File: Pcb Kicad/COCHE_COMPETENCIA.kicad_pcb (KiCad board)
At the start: 2 copper layers, 95 x 62 mm, 39 parts, among them J1 BAT, J2 SWITCH, J4 M1, J5 M2, J6 SENSORES, Q1 2N3904, SW1 SW_Push, SW2 SW_Push, U2 ESP32-DEVKIT-V1, U3 DRV8833, U4 DRV8833, U5 AMS1117

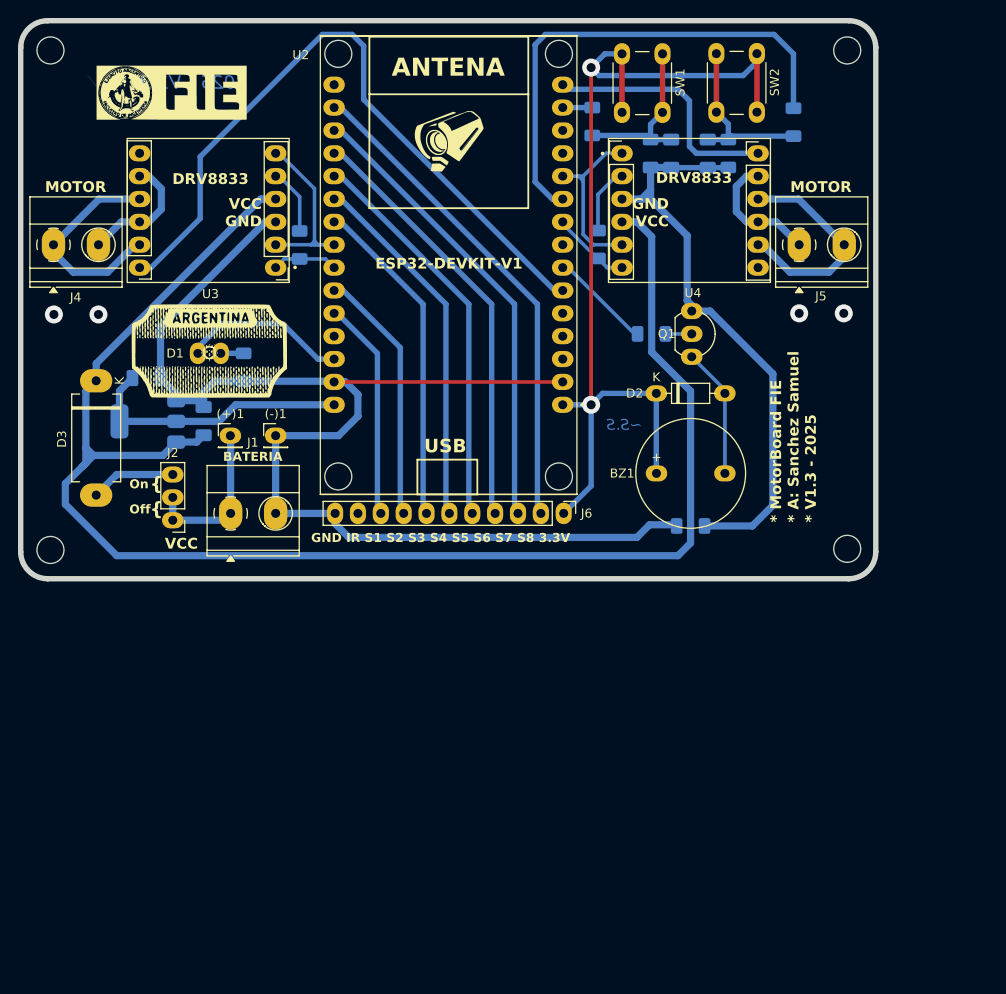
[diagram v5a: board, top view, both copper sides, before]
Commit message: V1.4 - Mejores pistas & Modulo de Interrupciones
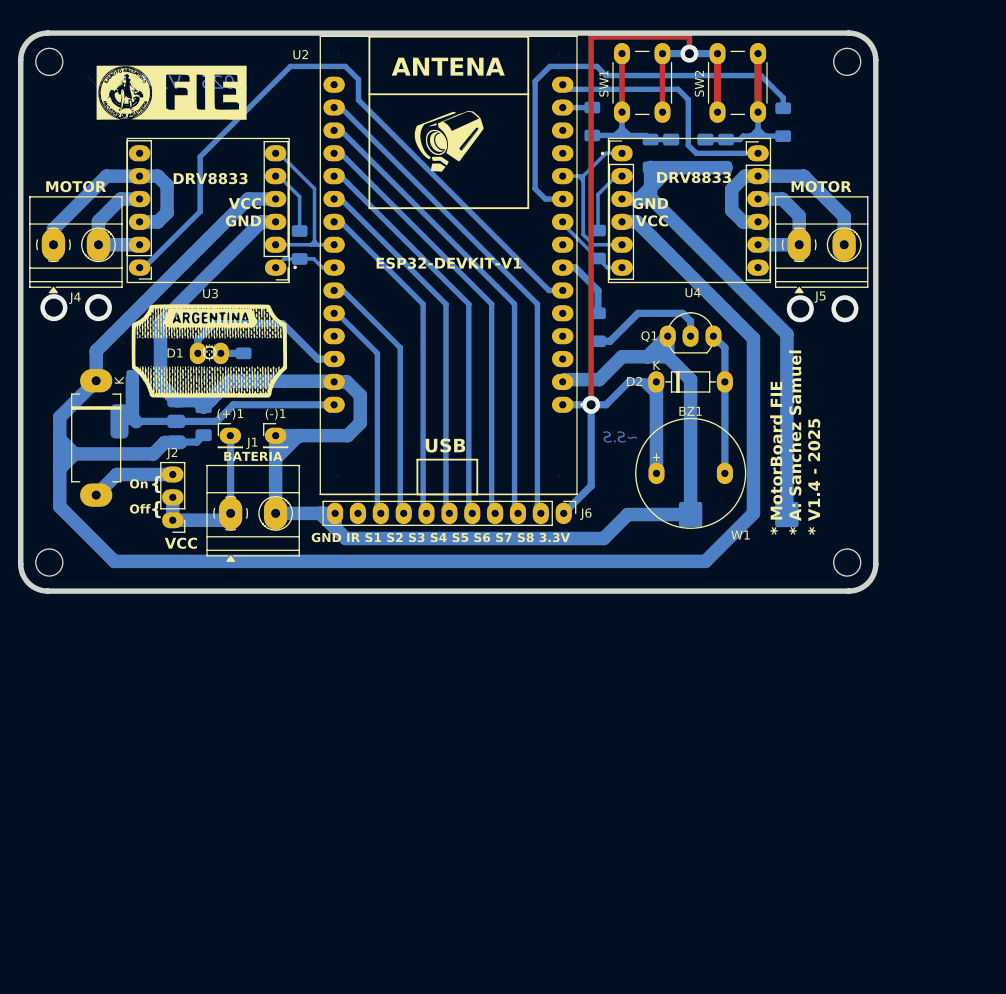
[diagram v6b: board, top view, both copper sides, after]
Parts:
- removed R1: 0, Resistor_SMD:R_1206_3216Metric_Pad1.30x1.75mm_HandSolder
- added W1: 5104, JUMPLER 5104:KEYSTONE_5104, B.Cu at (177.4, 79.1)
- moved SW1 7.92 mm to (169.0, 27.9), turned to -90 degrees
- moved SW2 7.83 mm to (175.1, 34.4), turned to 90 degrees
- moved R7 5.99 mm to (161.8, 58.3), turned to -90 degrees
- moved Q1 3.86 mm to (169.5, 59.3), turned to 0 degrees
- moved H4 1.52 mm to (189.5, 84.5)
- moved H3 1.40 mm to (100.8, 84.5)
- moved H1 1.28 mm to (100.8, 28.8)
- moved D2 1.27 mm to (168.3, 64.4)
- moved H2 1.27 mm to (189.5, 28.8)
- moved R8 1.14 mm to (182.4, 35.5)
- moved C4 0.25 mm to (173.7, 39.0)
- moved R3 0.25 mm to (176.0, 39.0)
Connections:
- U3 pad 10: Net-(J4-Pin_2) -> Net-(J4-Pin_1)
- U3 pad 11: Net-(J4-Pin_1) -> Net-(J4-Pin_2)
- U3 pad 8: Net-(J4-Pin_2) -> Net-(J4-Pin_1)
- U3 pad 9: Net-(J4-Pin_1) -> Net-(J4-Pin_2)
- U4 pad 10: Net-(J5-Pin_2) -> Net-(J5-Pin_1)
- U4 pad 11: Net-(J5-Pin_1) -> Net-(J5-Pin_2)
- U4 pad 8: Net-(J5-Pin_2) -> Net-(J5-Pin_1)
- U4 pad 9: Net-(J5-Pin_1) -> Net-(J5-Pin_2)
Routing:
- net GND: track 208.9 -> 226.8 mm
- net VCC: track 172.8 -> 189.0 mm
- net Net-(Q1-B): track 2.92 -> 13.6 mm
- net /SW2: track 55.2 -> 46.3 mm
- net /SLEEP_M1: track 77.0 -> 71.5 mm
- net /BUZZER: track 12.6 -> 9.37 mm
- net +3.3V: track 108.0 -> 110.3 mm
- net Net-(BZ1--): track 14.5 -> 15.8 mm
- net Net-(J4-Pin_2): track 13.9 -> 12.8 mm
- net Net-(J5-Pin_1): track 14.2 -> 13.1 mm
- net Net-(C3-Pad1): track 19.6 -> 20.3 mm
- net Net-(J5-Pin_2): track 24.6 -> 23.9 mm
- net Net-(C4-Pad1): track 19.8 -> 20.4 mm
- net /LED_LARGADA: track 18.5 -> 19.0 mm
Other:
- board text added: "* MotorBoard FIE * A: Sanchez Samuel * V1.4 - 2025"
- board text added: "2025 - V1.4"
- board text removed: "* MotorBoard FIE * A: Sanchez Samuel * V1.3 - 2025"
- board text removed: "2025 - V1.3"

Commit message: V1.4 - Programa seguidor Modular
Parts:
- moved R7 2.12 mm to (163.3, 56.8), turned to 0 degrees
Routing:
- net GND: track 226.8 -> 210.8 mm
- net Net-(Q1-B): track 13.6 -> 9.27 mm
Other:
- board text added: "* MotorBoard FIE * A: Sanchez Samuel * V1.5 - 2025"
- board text removed: "* MotorBoard FIE * A: Sanchez Samuel * V1.4 - 2025"
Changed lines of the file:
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@@
 	(footprint "Resistor_SMD:R_1206_3216Metric_Pad1.30x1.75mm_HandSolder"
 		(layer "B.Cu")
-		(at 161.798 58.319 -90)
+		(at 163.2972 56.8198)
 		(descr "Resistor SMD 1206 (3216 Metric), square (rectangular) end terminal, IPC_7351 nominal with elongated pad for handsoldering. (Body size source: IPC-SM-782 page 72, https://www.pcb-3d.com/wordpress/wp-content/uploads/ipc-sm-782a_amendment_1_and_2.pdf), generated with kicad-footprint-generator")
 		(tags "resistor handsolder")
 		(property "Reference" "R7"
-			(at 3.2252 0 180)
+			(at 3.2252 0 90)
 			(layer "B.SilkS")
 			(effects
@@
 		)
 		(property "Value" "1k"
-			(at 3.1236 0 180)
+			(at 3.1236 0 90)
 			(layer "B.Fab")
 			(effects
@@
 		)
 		(property "Datasheet" ""
-			(at 0 0 90)
+			(at 0 0 180)
 			(unlocked yes)
 			(layer "B.Fab")
@@
 		)
 		(property "Description" "Resistor"
-			(at 0 0 90)
+			(at 0 0 180)
 			(unlocked yes)
 			(layer "B.Fab")
@@
 		(attr smd)
 		(fp_line
-			(start -0.727064 0.91)
-			(end 0.727064 0.91)
+			(start -0.727064 -0.91)
+			(end 0.727064 -0.91)
 			(stroke
 				(width 0.12)
@@
 		)
 		(fp_line
-			(start -0.727064 -0.91)
-			(end 0.727064 -0.91)
+			(start -0.727064 0.91)
+			(end 0.727064 0.91)
 			(stroke
 				(width 0.12)
@@
 		)
 		(fp_line
-			(start -2.45 1.12)
-			(end 2.45 1.12)
+			(start -2.45 -1.12)
+			(end -2.45 1.12)
 			(stroke
 				(width 0.05)
@@
 		)
 		(fp_line
-			(start 2.45 1.12)
-			(end 2.45 -1.12)
+			(start -2.45 1.12)
+			(end 2.45 1.12)
 			(stroke
 				(width 0.05)
@@
 		)
 		(fp_line
-			(start -2.45 -1.12)
-			(end -2.45 1.12)
+			(start 2.45 -1.12)
+			(end -2.45 -1.12)
 			(stroke
 				(width 0.05)
@@
 		)
 		(fp_line
-			(start 2.45 -1.12)
-			(end -2.45 -1.12)
+			(start 2.45 1.12)
+			(end 2.45 -1.12)
 			(stroke
 				(width 0.05)
@@
 		)
 		(fp_line
-			(start -1.6 0.8)
-			(end 1.6 0.8)
+			(start -1.6 -0.8)
+			(end -1.6 0.8)
 			(stroke
 				(width 0.1)
@@
 		)
 		(fp_line
-			(start 1.6 0.8)
-			(end 1.6 -0.8)
+			(start -1.6 0.8)
+			(end 1.6 0.8)
 			(stroke
 				(width 0.1)
@@
 		)
 		(fp_line
-			(start -1.6 -0.8)
-			(end -1.6 0.8)
+			(start 1.6 -0.8)
+			(end -1.6 -0.8)
 			(stroke
 				(width 0.1)
@@
 		)
 		(fp_line
-			(start 1.6 -0.8)
-			(end -1.6 -0.8)
+			(start 1.6 0.8)
+			(end 1.6 -0.8)
 			(stroke
 				(width 0.1)
@@
 		)
 		(fp_text user "${REFERENCE}"
-			(at 0 0 90)
+			(at 0 0 0)
 			(layer "B.Fab")
 			(effects
@@
 		)
 		(pad "1" smd roundrect
-			(at -1.55 0 270)
+			(at -1.55 0)
 			(size 1.3 1.75)
 			(layers "B.Cu" "B.Mask" "B.Paste")
@@
 		)
 		(pad "2" smd roundrect
-			(at 1.55 0 270)
+			(at 1.55 0)
 			(size 1.3 1.75)
 			(layers "B.Cu" "B.Mask" "B.Paste")
@@
 		)
 	)
-	(gr_text "* MotorBoard FIE\n* A: Sanchez Samuel\n* V1.4 - 2025"
+	(gr_text "* MotorBoard FIE\n* A: Sanchez Samuel\n* V1.5 - 2025"
 		(at 183.769 81.407 90)
 		(layer "F.SilkS")
@@
 	)
 	(segment
-		(start 169.545 59.309)
-		(end 167.259 61.595)
-		(width 1.5)
-		(layer "B.Cu")
-		(net 7)
-	)
-	(segment
 		(start 133.788 81.788)
 		(end 132.588 80.588)
@@
 	)
 	(segment
-		(start 167.259 61.595)
-		(end 169.545 61.595)
-		(width 1.5)
-		(layer "B.Cu")
-		(net 7)
-	)
-	(segment
-		(start 157.877 64.389)
-		(end 158.131 64.135)
-		(width 1.5)
-		(layer "B.Cu")
-		(net 7)
-	)
-	(segment
 		(start 118.696 66.47)
 		(end 118.872 66.294)
@@
 	)
 	(segment
-		(start 164.465 61.595)
-		(end 167.259 61.595)
-		(width 1.5)
-		(layer "B.Cu")
-		(net 7)
-	)
-	(segment
 		(start 132.531 80.588)
 		(end 130.937 78.994)
@@
 	)
 	(segment
-		(start 158.131 64.135)
-		(end 161.925 64.135)
-		(width 1.5)
-		(layer "B.Cu")
-		(net 7)
-	)
-	(segment
-		(start 161.925 64.135)
-		(end 164.465 61.595)
-		(width 1.5)
-		(layer "B.Cu")
-		(net 7)
-	)
-	(segment
 		(start 120.852 64.314)
 		(end 122.428 64.314)
@@
 		(start 171.958 26.035)
 		(end 161.036 26.035)
-		(width 0.6)
+		(width 0.8)
 		(layer "F.Cu")
 		(net 17)
@@
 		(start 171.958 27.917)
 		(end 171.958 26.035)
-		(width 0.6)
+		(width 0.8)
 		(layer "F.Cu")
 		(net 17)
@@
 		(start 161.036 26.035)
 		(end 161.036 66.929)
-		(width 0.6)
+		(width 0.8)
 		(layer "F.Cu")
 		(net 17)
@@
 		(start 168.295 66.04)
 		(end 168.295 64.409)
-		(width 1.5)
+		(width 0.8)
 		(layer "B.Cu")
 		(net 17)
@@
 		(start 168.295 74.549)
 		(end 168.295 66.04)
-		(width 1.5)
+		(width 0.8)
 		(layer "B.Cu")
 		(net 17)
@@
 		(start 168.295 64.409)
 		(end 168.275 64.389)
-		(width 1.5)
+		(width 0.8)
 		(layer "B.Cu")
 		(net 17)
@@
 	)
 	(segment
+		(start 161.7472 54.1782)
+		(end 161.7472 56.8198)
+		(width 0.8)
+		(layer "B.Cu")
+		(net 28)
+	)
+	(segment
 		(start 157.877 51.689)
 		(end 158.242 51.689)
@@
 	)
 	(segment
-		(start 161.798 56.769)
-		(end 161.798 54.229)
+		(start 161.1376 53.5686)
+		(end 159.258 51.689)
 		(width 0.8)
 		(layer "B.Cu")
@@
 	(segment
 		(start 161.798 54.229)
-		(end 159.258 51.689)
+		(end 161.1376 53.5686)
 		(width 0.8)
 		(layer "B.Cu")
@@
 	)
 	(segment
-		(start 171.196 56.769)
-		(end 172.085 57.658)
+		(start 164.8472 56.8198)
+		(end 171.2468 56.8198)
 		(width 0.8)
 		(layer "B.Cu")
@@
 	(segment
 		(start 172.085 57.658)
-		(end 172.085 59.309)
-		(width 0.8)
-		(layer "B.Cu")
-		(net 42)
-	)
-	(segment
-		(start 163.143 59.869)
-		(end 166.243 56.769)
+		(end 171.2214 56.7944)
 		(width 0.8)
 		(layer "B.Cu")
@@
 	)
 	(segment
-		(start 166.243 56.769)
-		(end 171.196 56.769)
-		(width 0.8)
-		(layer "B.Cu")
-		(net 42)
-	)
-	(segment
-		(start 161.798 59.869)
-		(end 163.143 59.869)
+		(start 172.085 59.309)
+		(end 172.085 57.658)
 		(width 0.8)
 		(layer "B.Cu")

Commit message: V2.0 - Nueva version Seguidor De Linea
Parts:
- removed (+)1, (-)1: TestPoint, Connector_PinHeader_2.54mm:PinHeader_1x01_P2.54mm_Vertical
- removed BZ1: Buzzer, Buzzer_Beeper:MagneticBuzzer_ProSignal_ABI-009-RC
- removed C4: 100n, Capacitor_SMD:C_1206_3216Metric_Pad1.33x1.80mm_HandSolder
- removed D2: 1N4148, Diode_THT:D_DO-35_SOD27_P7.62mm_Horizontal
- removed D3: 1N5822, Diode_THT:D_DO-201AD_P12.70mm_Horizontal
- removed H1, H2, H3, H4: MountingHole, MountingHole:MountingHole_3mm
- removed J2: SWITCH, Connector_PinHeader_2.54mm:PinHeader_1x03_P2.54mm_Vertical
- removed J4: M1, TerminalBlock_Phoenix:TerminalBlock_Phoenix_MKDS-1,5-2_1x02_P5.00mm_Horizontal
- removed Q1: 2N3904, Package_TO_SOT_THT:TO-92_Inline_Wide
- removed R2, R3: 10k, Resistor_SMD:R_1206_3216Metric_Pad1.30x1.75mm_HandSolder
- removed R4: 220, Resistor_SMD:R_1206_3216Metric_Pad1.30x1.75mm_HandSolder
- removed R5, R6: 0, Resistor_SMD:R_1206_3216Metric_Pad1.30x1.75mm_HandSolder
- removed R7: 1k, Resistor_SMD:R_1206_3216Metric_Pad1.30x1.75mm_HandSolder
- removed R8, R9: 100, Resistor_SMD:R_1206_3216Metric_Pad1.30x1.75mm_HandSolder
- removed U3, U4: DRV8833, DRV8833:DRV8833
- removed U5: AMS1117, Package_TO_SOT_SMD:SOT-223-3_TabPin2
- removed W1: 5104, JUMPLER 5104:KEYSTONE_5104
- added BT1: 2S 70C 250mAH, Bateria_9S:Bateria_Lado, F.Cu at (167.4, 102.7)
- added J3: SENSORES, Connector_PinHeader_2.54mm:PinHeader_1x11_P2.54mm_Vertical, F.Cu at (180.1, 68.4)
- added M1: Pololu DC, PololuLibrary:pololu, F.Cu at (154.1, 117.4)
- added M2: Pololu DC, PololuLibrary:pololu, F.Cu at (180.8, 117.4)
- added U1: DRV8833, DRV8833:DRV8833, F.Cu at (135.3, 84.3)
- C2: value 1u -> 100n
- D1: value LED_RED -> D_Schottky; footprint LED_THT:LED_D5.0mm -> Diode_THT:D_DO-35_SOD27_P7.62mm_Horizontal
- J1: footprint TerminalBlock_Phoenix:TerminalBlock_Phoenix_MKDS-1,5-2_1x02_P5.00mm_Horizontal -> Connector_AMASS:AMASS_XT30UPB-M_1x02_P5.0mm_Vertical
- J5: value M2 -> M1; footprint TerminalBlock_Phoenix:TerminalBlock_Phoenix_MKDS-1,5-2_1x02_P5.00mm_Horizontal -> Connector_PinHeader_2.54mm:PinHeader_1x02_P2.54mm_Vertical
- J6: value SENSORES -> M2; footprint Connector_PinHeader_2.54mm:PinHeader_1x11_P2.54mm_Vertical -> Connector_PinHeader_2.54mm:PinHeader_1x02_P2.54mm_Vertical
- SW1: value SW_Push -> ON/OFF; footprint Button_Switch_THT:SW_PUSH_6mm_H5mm -> switch6P:SWITCH_6PINS
- SW2: value SW_Push -> SW_RUN
- U2: value ESP32-DEVKIT-V1 -> ARDUINO_NANO; footprint ESP32-DEVKIT-V1:MODULE_ESP32_DEVKIT_V1 -> Arduino NANO:MODULE_ARDUINO_NANO
- moved G*** 110.3 mm to (188.5, 107.1)
- moved G*** 79.9 mm to (167.4, 124.3)
- moved G*** 79.6 mm to (175.2, 83.7)
- moved C3 78.7 mm to (177.2, 117.4)
- moved J5 70.9 mm to (160.7, 116.1)
- moved SW2 70.6 mm to (195.4, 102.0)
- moved C2 70.5 mm to (157.6, 117.4), turned to -90 degrees
- moved C1 56.4 mm to (167.6, 95.6), turned to -90 degrees
- moved SW1 52.0 mm to (138.8, 70.2), turned to 0 degrees
- moved G*** 46.4 mm to (145.2, 84.1)
- moved U2 44.2 mm to (175.2, 83.9), turned to 90 degrees
- moved J6 42.8 mm to (174.1, 118.7), turned to 180 degrees
- moved D1 27.3 mm to (135.2, 83.9), turned to -90 degrees
- moved J1 26.5 mm to (135.2, 101.3), turned to 90 degrees
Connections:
- C1 pad 1: VCC -> /SW1
- C1 pad 2: GND -> GND_BAT
- C2 pad 1: +5V -> /OUT1-
- C2 pad 2: GND -> /OUT1+
- C3 pad 1: Net-(C3-Pad1) -> /OUT2+
- C3 pad 2: GND -> /OUT2-
- D1 pad 2: /LED_LARGADA -> /BAT+
- J1 pad 1: Net-(J1-Pin_1) -> GND_BAT
- J1 pad 2: GND -> /BAT+
- J5 pad 1: Net-(J5-Pin_1) -> /OUT1-
- J5 pad 2: Net-(J5-Pin_2) -> /OUT1+
- J6 pad 1: +3.3V -> /OUT2-
- J6 pad 2: /S8 -> /OUT2+
- SW1 pad 1: +3.3V -> unconnected-(SW1-A-Pad1)
- SW1 pad 2: Net-(C3-Pad1) -> VCC
- SW2 pad 1: +3.3V -> /SW1
- SW2 pad 2: Net-(C4-Pad1) -> GND_BAT
- U2 pad 1: +3.3V -> /TX
- U2 pad 10: /SW2 -> unconnected-(U2-D7-Pad10)
- U2 pad 11: /IN_M2_A -> unconnected-(U2-D8-Pad11)
- U2 pad 12: unconnected-(U2-RX0-Pad12) -> /IN_M1_B
- U2 pad 13: unconnected-(U2-TX0-Pad13) -> /IN_M1_A
- U2 pad 14: /SW1 -> unconnected-(U2-D11/MOSI-Pad14)
- U2 pad 15: /SLEEP_M2 -> unconnected-(U2-D12/MISO-Pad15)
- U2 pad 16: unconnected-(U2-EN-Pad16) -> /LED_LARGADA
- U2 pad 17: /S8 -> +3.3V
- U2 pad 18: /S7 -> unconnected-(U2-AREF-Pad18)
- U2 pad 19: /S6 -> /S8
- U2 pad 2: GND -> /RX
- U2 pad 20: /S5 -> /S7
- U2 pad 21: /S4 -> /S6
- U2 pad 22: /S3 -> /S5
- U2 pad 23: /IN_M1_B -> /S4
- U2 pad 24: /IN_M1_A -> /S3
- U2 pad 27: unconnected-(U2-D12-Pad27) -> +5.0V
- U2 pad 28: /LED_LARGADA -> unconnected-(U2-RESET-Pad28)
- U2 pad 30: +5V -> VCC
- U2 pad 4: unconnected-(U2-D2-Pad4) -> GND_BAT
- U2 pad 5: unconnected-(U2-D4-Pad5) -> /SW1
- U2 pad 6: /SLEEP_M1 -> /SLEEP
- U2 pad 7: /BUZZER -> unconnected-(U2-D4-Pad7)
- U2 pad 8: unconnected-(U2-D5-Pad8) -> /IN_M2_B
- U2 pad 9: /IN_M2_B -> /IN_M2_A
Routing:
- net GND_BAT: track 0.00 -> 212.1 mm
- net GND: track 210.8 -> 10.0 mm
- net VCC: track 189.0 -> 31.8 mm
- net +3.3V: track 110.3 -> 14.3 mm, vias 2 -> 0
- net /SLEEP_M1: track 71.5 -> 0.00 mm
- net /OUT2-: track 0.00 -> 48.0 mm
- net /OUT1+: track 0.00 -> 46.3 mm
- net /SW2: track 46.3 -> 0.00 mm
- net /S8: track 55.0 -> 11.1 mm
- net /OUT2+: track 0.00 -> 43.4 mm
- net /IN_M1_A: track 7.29 -> 49.1 mm
- net /IN_M2_B: track 8.89 -> 49.8 mm
- net /S7: track 51.4 -> 11.1 mm
- net /OUT1-: track 0.00 -> 39.7 mm
- net /S6: track 47.9 -> 11.1 mm
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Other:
- board size 95 x 62 mm -> 75 x 65 mm
- board text added: "+ -"
- board text added: "2026 - V2.0"
- board text added: "MotorBoard FIE * A: Sanchez Samuel * V2.0 - 2026 *"
- board text added: "usb"
- board text removed: "* MotorBoard FIE * A: Sanchez Samuel * V1.5 - 2025"
- board text removed: "2025 - V1.4"
- board text removed: "ANTENA"
- board text removed: "BATERIA"
- board text removed: "DRV8833"
- board text removed: "ESP32-DEVKIT-V1"
- board text removed: "GND IR S1 S2 S3 S4 S5 S6 S7 S8 3.3V"
- board text removed: "GND VCC"
- board text removed: "MOTOR"
- board text removed: "Off"
- board text removed: "On"
- board text removed: "USB"
- board text removed: "VCC"
- board text removed: "VCC GND"
- board text removed: "{"
